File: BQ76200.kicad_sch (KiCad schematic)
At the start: 37 parts, among them Q1 IPT012N08N5, Q2 IPT012N08N5, Q3 IPT012N08N5, Q4 IPT012N08N5, Q5 IPT012N08N5, Q6 IPT012N08N5, Q7 IPT012N08N5, Q8 IPT012N08N5, Q9 IPT012N08N5, U1 BQ76200PW

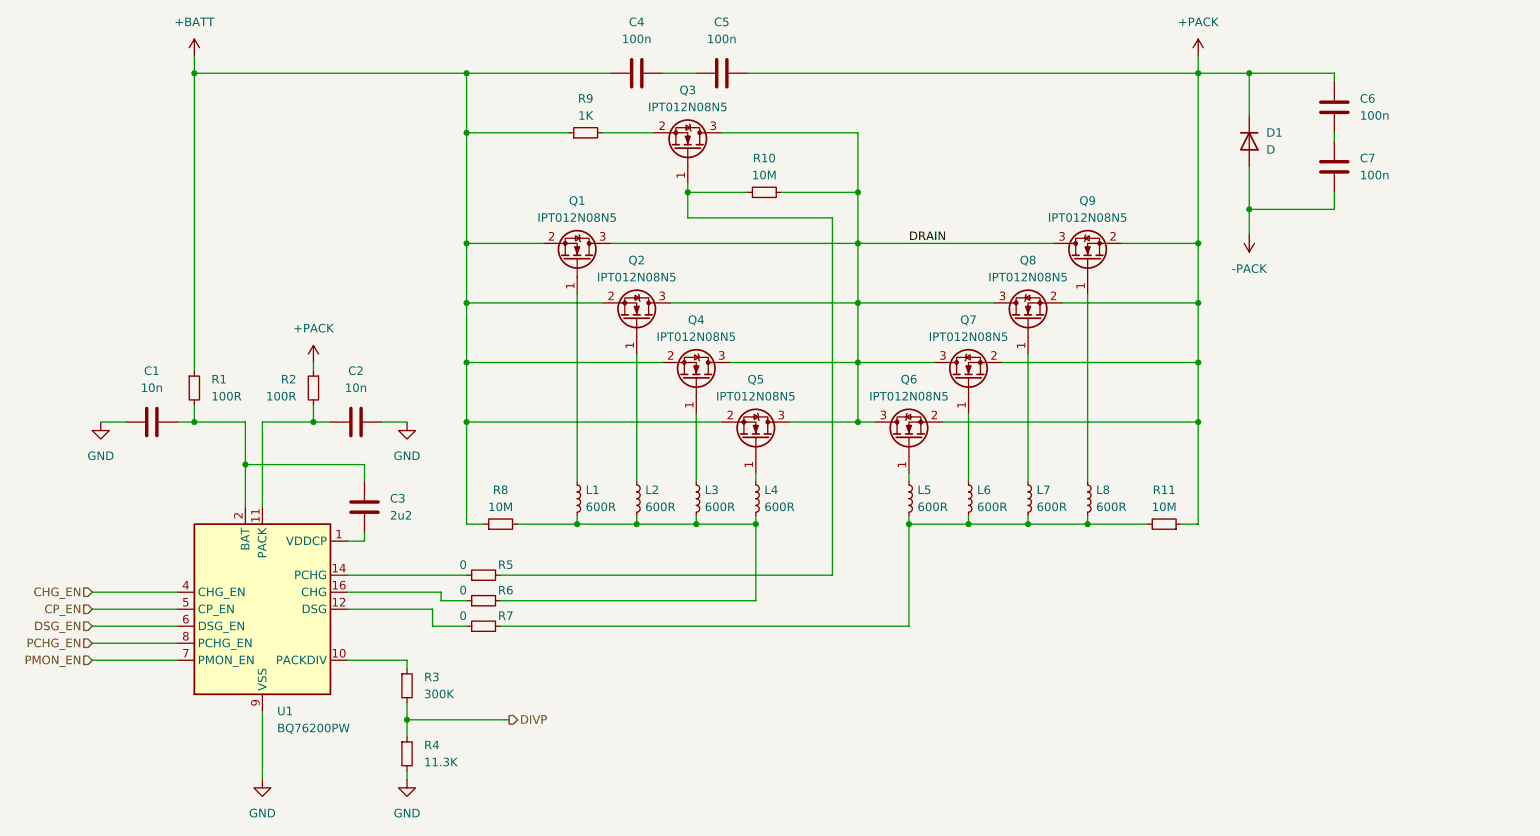
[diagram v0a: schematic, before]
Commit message: Changes Mosfet's package to D2PAK
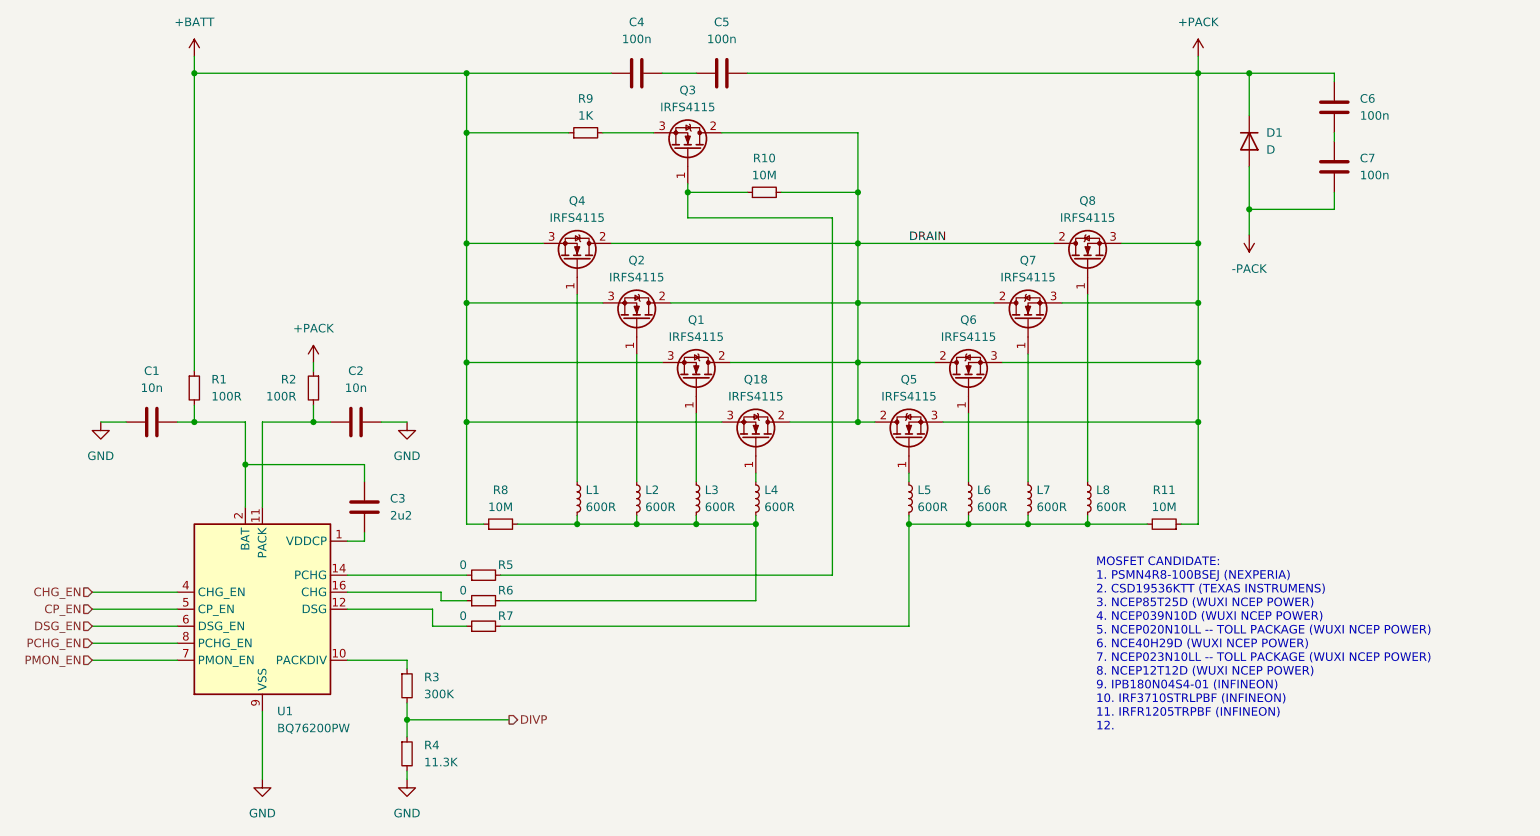
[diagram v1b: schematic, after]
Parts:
- removed Q1, Q2, Q3, Q4, Q5, Q6, Q7, Q8, Q9: IPT012N08N5, Package_TO_SOT_SMD:Infineon_PG-HSOF-8-1, symbol Transistor_FET:IPT012N08N5
- added Q1, Q18, Q2, Q3, Q4, Q5, Q6, Q7, Q8: IRFS4115, Package_TO_SOT_SMD:TO-263-2, symbol Transistor_FET:IRFS4115
- C1, C2, C4, C5, C6, C7: footprint (none) -> Capacitor_SMD:C_0603_1608Metric
- C3: footprint (none) -> Capacitor_SMD:C_0805_2012Metric
- D1: footprint (none) -> Diode_SMD:D_SMA
- L1, L2, L3, L4, L5, L6, L7, L8: footprint (none) -> Inductor_SMD:L_0805_2012Metric
- R1, R10, R11, R2, R3, R4, R5, R6, R7, R8, R9: footprint (none) -> Resistor_SMD:R_0603_1608Metric
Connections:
- net +BATT: now also Q1.3 (S), Q18.3 (S), Q2.3 (S), Q4.3 (S)
- net +PACK: now also Q5.3 (S), Q6.3 (S), Q7.3 (S), Q8.3 (S)
- net DRAIN: now also Q1.2 (D), Q18.2 (D), Q2.2 (D), Q3.2 (D), Q4.2 (D), Q5.2 (D), Q6.2 (D), Q7.2 (D), Q8.2 (D)
- net at L3.1: now also Q1.1 (G)
- net at L6.1: now also Q6.1 (G)
- net at L5.1: now also Q5.1 (G)
- net at L1.1: now also Q4.1 (G)
- net at L2.1: now also Q2.1 (G)
- net at L8.1: now also Q8.1 (G)
- net at R10.1, R5.2: now also Q3.1 (G)
- net at L7.1: now also Q7.1 (G)
- net at L4.1: now also Q18.1 (G)
- net at R9.2: now also Q3.3 (S)
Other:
- note added: "MOSFET CANDIDATE: 1. PSMN4R8-100BSEJ (NEXPERIA) 2. CSD19536KTT (TEXAS INSTRUMENS) 3. NCEP85T25D (WUXI NCEP POWER) 4. NCEP039N10D (WUXI NCEP POWER) 5. NCEP020N10LL -- TOLL PACKAGE (WUXI NCEP POWER) 6. NCE40H29D (WUXI NCEP POWER) 7. NCEP023N10LL -- TOLL PACKAGE (WUXI NCEP POWER) 8. NCEP12T12D (WUXI NCEP POWER) 9. IPB180N04S4-01 (INFINEON) 10. IRF3710STRLPBF (INFINEON) 11. IRFR1205TRPBF (INFINEON) 1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"
